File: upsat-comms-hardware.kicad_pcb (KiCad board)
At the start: 4 copper layers, 92.5 x 92.5 mm, 314 parts, among them U1 TXCO_TG_5021CG, U10 CC1120, U12 ADT7420, U14 OPA320, U16 RF5110G, U18 FA_128_, U2 TPS79930, U3 FA_128_, U4 CC1120, U5 STM32F407VG, U6 TXCO_TG_5021CG, U8 TPS79930, Y1 Crystal, Y2 Crystal

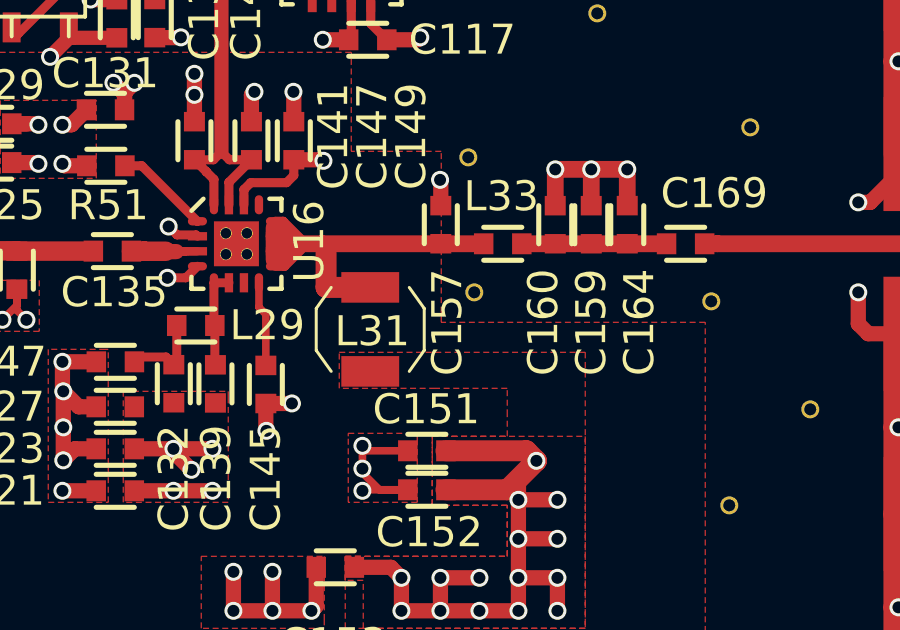
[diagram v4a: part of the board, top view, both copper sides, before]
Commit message: Fix Taiyo Yuden bead footprint and placement.
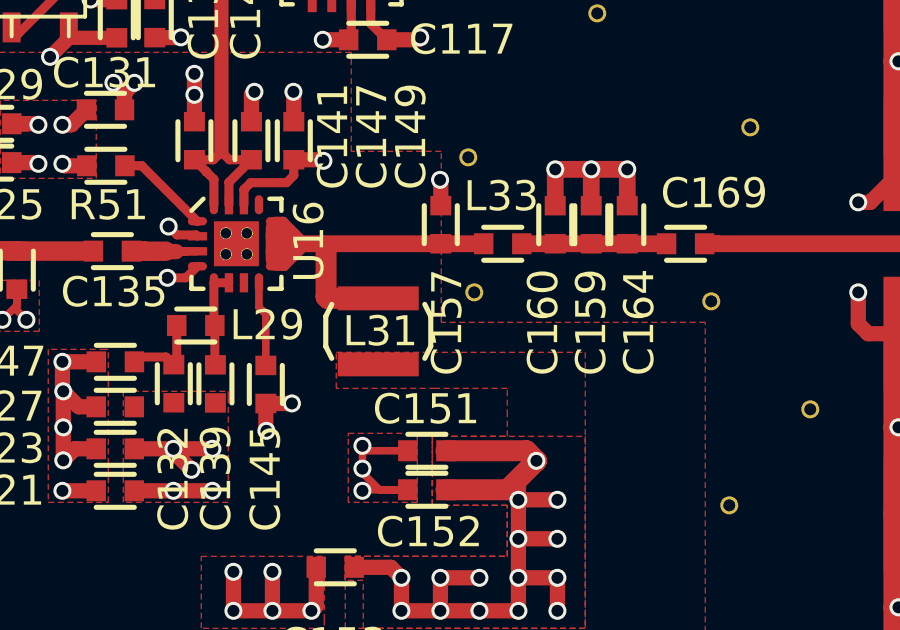
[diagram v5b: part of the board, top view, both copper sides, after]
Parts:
- moved L31 0.45 mm to (144.4, 78.4)
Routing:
- net Net-(C157-Pad2): track 19.9 -> 20.5 mm
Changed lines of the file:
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@@
     (links 583)
     (no_connects 1)
-    (area 102.424999 54.524999 195.075001 147.175001)
+    (area 99.034505 41.132869 335.031237 149.6)
     (thickness 1.55)
     (drawings 10345)
-    (tracks 1936)
+    (tracks 1938)
     (zones 0)
     (modules 314)
@@
   )
   (setup
-    (last_trace_width 0.508)
+    (last_trace_width 0.7)
     (user_trace_width 0.254)
     (user_trace_width 0.27)
@@
     (user_trace_width 0.508)
     (user_trace_width 0.56)
-    (user_trace_width 1.8)
+    (user_trace_width 0.7)
     (trace_clearance 0.1524)
     (zone_clearance 0.25)
@@
       (net 4 GND))
   )
-  (module libs:Taiyo_Yuden_bead (layer F.Cu)
-    (at 144.13238 78.035664 270)
-    (fp_text reference L31 (at 1.464336 -0.06762 360) (layer F.SilkS)
-      (effects (font (size 1 1) (thickness 0.17)))
-    )
-    (fp_text value "Taiyo Yuden " (at 2.064336 -4.66762 270) (layer F.SilkS) hide
-      (effects (font (size 0.6 0.6) (thickness 0.1)))
-    )
-    (fp_line (start 2.1 1.8) (end 2.8 1.3) (layer F.SilkS) (width 0.1))
-    (fp_line (start 0.7 1.8) (end 2.1 1.8) (layer F.SilkS) (width 0.1))
-    (fp_line (start 0 1.3) (end 0.7 1.8) (layer F.SilkS) (width 0.1))
-    (fp_line (start 2.1 -1.8) (end 2.8 -1.3) (layer F.SilkS) (width 0.1))
-    (fp_line (start 0.7 -1.8) (end 2.1 -1.8) (layer F.SilkS) (width 0.1))
-    (fp_line (start 0 -1.3) (end 0.7 -1.8) (layer F.SilkS) (width 0.1))
-    (pad 1 smd rect (at 0 0 270) (size 1.02 1.93) (layers F.Cu F.Paste F.Mask)
-      (net 61 "Net-(C157-Pad2)"))
-    (pad 2 smd rect (at 2.8 0 270) (size 1.02 1.93) (layers F.Cu F.Paste F.Mask)
-      (net 5 +3V3))
-  )
   (module libs:upsat-logo (layer F.Cu)
     (at 182.4 76 90)
@@
       (xy -3.63728 5.38988)) (layer F.SilkS) (width 0.00254))
   )
+  (module libs:Taiyo_Yuden_bead (layer F.Cu)
+    (at 144.4 78.4 270)
+    (fp_text reference L31 (at 1.1 -0.06762 360) (layer F.SilkS)
+      (effects (font (size 1 1) (thickness 0.17)))
+    )
+    (fp_text value "Taiyo Yuden " (at 1.1 0 270) (layer F.SilkS) hide
+      (effects (font (size 1 1) (thickness 0.17)))
+    )
+    (fp_line (start 1.6 1.75) (end 2 1.55) (layer F.SilkS) (width 0.17))
+    (fp_line (start 0.6 1.75) (end 1.6 1.75) (layer F.SilkS) (width 0.17))
+    (fp_line (start 0.2 1.55) (end 0.6 1.75) (layer F.SilkS) (width 0.17))
+    (fp_line (start 1.6 -1.75) (end 2 -1.55) (layer F.SilkS) (width 0.17))
+    (fp_line (start 0.6 -1.75) (end 1.6 -1.75) (layer F.SilkS) (width 0.17))
+    (fp_line (start 0.2 -1.55) (end 0.6 -1.75) (layer F.SilkS) (width 0.17))
+    (pad 1 smd rect (at 0 0 270) (size 0.8 2.7) (layers F.Cu F.Paste F.Mask)
+      (net 61 "Net-(C157-Pad2)"))
+    (pad 2 smd rect (at 2.2 0 270) (size 0.8 2.7) (layers F.Cu F.Paste F.Mask)
+      (net 5 +3V3))
+  )
   (gr_text "In memory of K. Efstathiou" (at 150 143.9) (layer B.SilkS)
     (effects (font (size 1.5 1.5) (thickness 0.3)) (justify mirror))
@@
   (segment (start 140.42238 78.695664) (end 140.42238 77.881328) (width 0.254) (layer F.Cu) (net 60))
   (segment (start 140.65238 80.635664) (end 140.65238 78.925664) (width 0.254) (layer F.Cu) (net 60))
+  (segment (start 144.4 78.4) (end 142.722969 78.4) (width 0.7) (layer F.Cu) (net 61))
+  (segment (start 142.722969 78.4) (end 142.717478 78.405491) (width 0.7) (layer F.Cu) (net 61))
+  (segment (start 142.717478 78.405491) (end 142.65938 78.347393) (width 0.7) (layer F.Cu) (net 61))
+  (segment (start 142.65938 78.347393) (end 142.65938 76.86062) (width 0.7) (layer F.Cu) (net 61))
   (segment (start 141.42 76.94) (end 141.247994 77.112006) (width 0.3) (layer F.Cu) (net 61))
   (segment (start 141.247994 77.112006) (end 140.97238 77.112006) (width 0.3) (layer F.Cu) (net 61))
@@
   (segment (start 140.97238 76.565664) (end 142.364424 76.565664) (width 0.27) (layer F.Cu) (net 61))
   (segment (start 142.364424 76.565664) (end 142.65938 76.86062) (width 0.27) (layer F.Cu) (net 61))
-  (segment (start 142.65938 78.035664) (end 142.65938 76.86062) (width 0.7) (layer F.Cu) (net 61))
   (segment (start 140.97238 76.565664) (end 140.986716 76.58) (width 0.56) (layer F.Cu) (net 61))
   (segment (start 146.48476 76.58) (end 147.913432 76.58) (width 0.56) (layer F.Cu) (net 61))
   (segment (start 147.913432 76.58) (end 147.91476 76.581328) (width 0.56) (layer F.Cu) (net 61))
-  (segment (start 144.13238 78.035664) (end 142.65938 78.035664) (width 0.7) (layer F.Cu) (net 61))
   (segment (start 140.97238 76.831328) (end 140.97238 76.565664) (width 0.254) (layer F.Cu) (net 61))
   (segment (start 152.68 76.581328) (end 154.01 76.581328) (width 0.56) (layer F.Cu) (net 62))
@@
       (pts
         (xy 146.2 83) (xy 148.7 83) (xy 148.7 82.3) (xy 148.7 81.4) (xy 146.3 81.4)
-        (xy 143.1 81.4) (xy 143.1 80.2) (xy 151.3 80.2) (xy 151.3 89.4) (xy 143.3 89.4)
+        (xy 143 81.4) (xy 143 80.2) (xy 151.3 80.2) (xy 151.3 89.4) (xy 143.3 89.4)
         (xy 143.3 87) (xy 148.7 87) (xy 148.7 85.3) (xy 146.2 85.3) (xy 146.2 84.2)
       )

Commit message: add RF values for CC1120 RX, wrong path for mmcx con.
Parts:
- C31: value TBD -> 100 pF
- C32: value TBD -> 120 pF
- C34, C35, C37, C39: value TBD -> 15 pF
- C44: value TBD -> 18 pF
- C47: value TBD -> 1.8 pF
- L10: value TBD -> 75 nH
- L2: value TBD -> 150 nH
- L3: value TBD -> 180 nH
- L5: value TBD -> 19 nH
- L6, L7: value TBD -> 91 nH
- L8: value TBD -> 120 nH
- L9: value TBD -> 43 nH
- R19: value TBD -> 22 Ohm
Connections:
- U1 pad 1: (no net) -> Net-(U1-Pad1)
- U10 pad 16: (no net) -> Net-(U10-Pad16)
- U12 pad 10: (no net) -> Net-(U12-Pad10)
- U12 pad 13: (no net) -> Net-(U12-Pad13)
- U12 pad 14: (no net) -> Net-(U12-Pad14)
- U12 pad 15: (no net) -> Net-(U12-Pad15)
- U12 pad 16: (no net) -> Net-(U12-Pad16)
- U12 pad 5: (no net) -> Net-(U12-Pad5)
- U12 pad 6: (no net) -> Net-(U12-Pad6)
- U12 pad 7: (no net) -> Net-(U12-Pad7)
- U12 pad 8: (no net) -> Net-(U12-Pad8)
- U12 pad 9: (no net) -> Net-(U12-Pad9)
- U16 pad 13: (no net) -> Net-(U16-Pad13)
- U16 pad 7: (no net) -> Net-(U16-Pad7)
- U4 pad 16: (no net) -> Net-(U4-Pad16)
- U5 pad 1: (no net) -> Net-(U5-Pad1)
- U5 pad 15: (no net) -> Net-(U5-Pad15)
- U5 pad 16: (no net) -> Net-(U5-Pad16)
- U5 pad 17: (no net) -> Net-(U5-Pad17)
- U5 pad 18: (no net) -> Net-(U5-Pad18)
- U5 pad 2: (no net) -> Net-(U5-Pad2)
- U5 pad 23: (no net) -> Net-(U5-Pad23)
- U5 pad 24: (no net) -> Net-(U5-Pad24)
- U5 pad 29: (no net) -> Net-(U5-Pad29)
- U5 pad 3: (no net) -> Net-(U5-Pad3)
- U5 pad 33: (no net) -> Net-(U5-Pad33)
- U5 pad 34: (no net) -> Net-(U5-Pad34)
- U5 pad 35: (no net) -> Net-(U5-Pad35)
- U5 pad 37: (no net) -> Net-(U5-Pad37)
- U5 pad 39: (no net) -> Net-(U5-Pad39)
- U5 pad 4: (no net) -> Net-(U5-Pad4)
- U5 pad 41: (no net) -> Net-(U5-Pad41)
- U5 pad 42: (no net) -> Net-(U5-Pad42)
- U5 pad 43: (no net) -> Net-(U5-Pad43)
- U5 pad 44: (no net) -> Net-(U5-Pad44)
- U5 pad 45: (no net) -> Net-(U5-Pad45)
- U5 pad 5: (no net) -> Net-(U5-Pad5)
- U5 pad 55: (no net) -> Net-(U5-Pad55)
- U5 pad 56: (no net) -> Net-(U5-Pad56)
- U5 pad 57: (no net) -> Net-(U5-Pad57)
- U5 pad 58: (no net) -> Net-(U5-Pad58)
- U5 pad 59: (no net) -> Net-(U5-Pad59)
- U5 pad 60: (no net) -> Net-(U5-Pad60)
- U5 pad 61: (no net) -> Net-(U5-Pad61)
- U5 pad 62: (no net) -> Net-(U5-Pad62)
- U5 pad 63: (no net) -> Net-(U5-Pad63)
- U5 pad 64: (no net) -> Net-(U5-Pad64)
- U5 pad 65: (no net) -> Net-(U5-Pad65)
- U5 pad 66: (no net) -> Net-(U5-Pad66)
- U5 pad 68: (no net) -> Net-(U5-Pad68)
- U5 pad 7: (no net) -> Net-(U5-Pad7)
- U5 pad 70: (no net) -> Net-(U5-Pad70)
- U5 pad 71: (no net) -> Net-(U5-Pad71)
- U5 pad 78: (no net) -> Net-(U5-Pad78)
- U5 pad 79: (no net) -> Net-(U5-Pad79)
- U5 pad 81: (no net) -> Net-(U5-Pad81)
- U5 pad 82: (no net) -> Net-(U5-Pad82)
- U5 pad 85: (no net) -> Net-(U5-Pad85)
- U5 pad 86: (no net) -> Net-(U5-Pad86)
- U5 pad 87: (no net) -> Net-(U5-Pad87)
- U5 pad 88: (no net) -> Net-(U5-Pad88)
- U5 pad 90: (no net) -> Net-(U5-Pad90)
- U5 pad 91: (no net) -> Net-(U5-Pad91)
- U5 pad 92: (no net) -> Net-(U5-Pad92)
- U5 pad 93: (no net) -> Net-(U5-Pad93)
- U5 pad 97: (no net) -> Net-(U5-Pad97)
- U5 pad 98: (no net) -> Net-(U5-Pad98)
- U6 pad 1: (no net) -> Net-(U6-Pad1)

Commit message: add power amp RF out component values, add comments on CC1120 TXCO-Crystal section, add comments on CC1120 regulator-bead
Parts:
- C160: value 22-30pF -> 22 pF
- C31: value 100 pF -> 150 pF
- C32: value 120 pF -> 100 pF
- L33: value 2.7-3.9nH -> 2.7 nH
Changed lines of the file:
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@@
 (kicad_pcb (version 4) (host pcbnew 4.0.2-1.fc23-product)
   (general
-    (links 583)
-    (no_connects 1)
+    (links 600)
+    (no_connects 15)
     (area 102.424999 54.524999 195.075001 147.175001)
     (thickness 1.55)
@@
     (add_net "Net-(P2-Pad4)")
     (add_net "Net-(P2-Pad5)")
+    (add_net "Net-(P2-Pad6)")
     (add_net "Net-(R17-Pad1)")
     (add_net "Net-(R20-Pad1)")
@@
       (effects (font (size 1 1) (thickness 0.17)))
     )
-    (fp_text value "100 pF" (at 3.9 0 270) (layer F.SilkS) hide
+    (fp_text value "150 pF" (at 3.9 0 270) (layer F.SilkS) hide
       (effects (font (size 1 1) (thickness 0.17)))
     )
@@
       (effects (font (size 1 1) (thickness 0.17)))
     )
-    (fp_text value "120 pF" (at 3.9 0 90) (layer F.SilkS) hide
+    (fp_text value "100 pF" (at 3.9 0 90) (layer F.SilkS) hide
       (effects (font (size 1 1) (thickness 0.17)))
     )
@@
       (effects (font (size 1 1) (thickness 0.17)))
     )
-    (fp_text value 2.7-3.9nH (at 0.61 1.18 180) (layer F.SilkS) hide
+    (fp_text value "2.7 nH" (at 0.61 1.18 180) (layer F.SilkS) hide
       (effects (font (size 0.5 0.5) (thickness 0.1)))
     )
@@
       (effects (font (size 1 1) (thickness 0.17)))
     )
-    (fp_text value 22-30pF (at 0.61 1.18 90) (layer F.SilkS) hide
+    (fp_text value "22 pF" (at 0.61 1.18 90) (layer F.SilkS) hide
       (effects (font (size 0.5 0.5) (thickness 0.1)))
     )
